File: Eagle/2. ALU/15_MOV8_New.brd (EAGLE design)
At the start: 160 x 100 mm, 7 parts, among them IC3 74LS126N, IC4 74LS126N

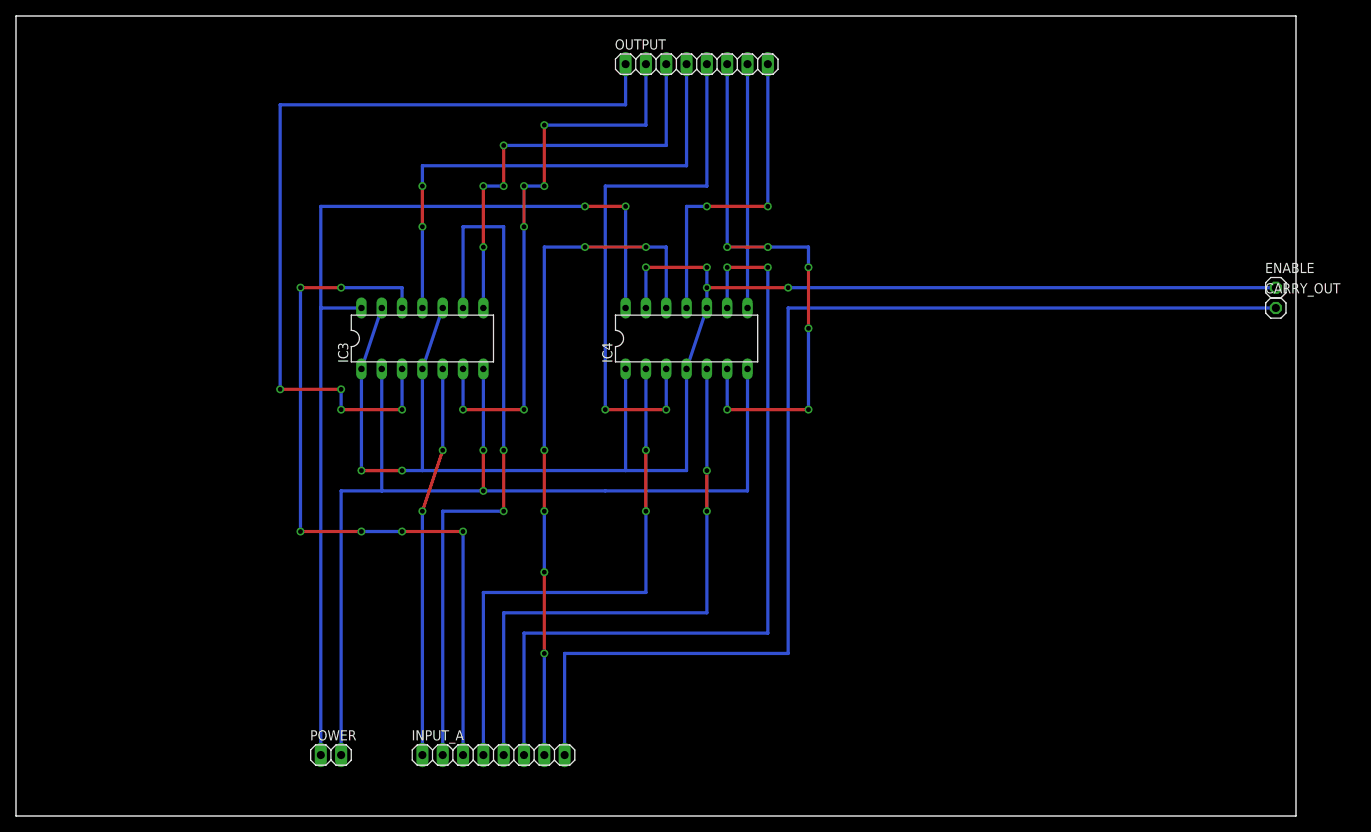
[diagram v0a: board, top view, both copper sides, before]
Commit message: Added new schematics.
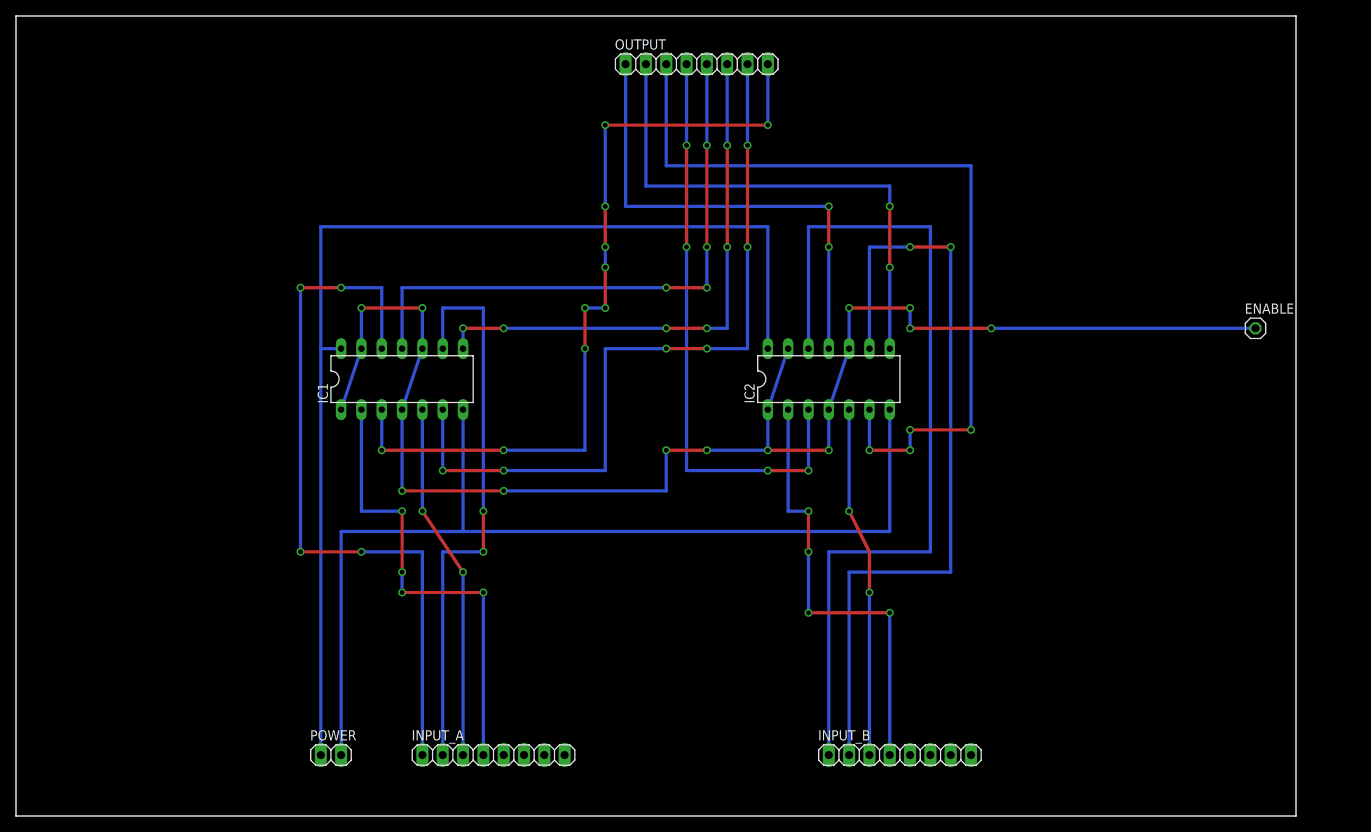
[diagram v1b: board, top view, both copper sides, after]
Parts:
- removed CARRY_OUT: (no value), pinhead:1X01
- removed IC3, IC4: 74LS126N, 74xx-eu:DIL14
- added IC1, IC2: 74LS126N, 74xx-eu:DIL14
- added INPUT_B: (no value), pinhead:1X08
- moved ENABLE 5.68 mm to (154.9, 61.0)
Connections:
- removed net N$20: IC3.12, INPUT_A.3
- removed net N$21: IC4.2, INPUT_A.4
- removed net N$25: IC3.3, OUTPUT.1
- removed net N$26: IC3.6, OUTPUT.2
- removed net N$27: IC3.8, OUTPUT.3
- removed net N$28: IC3.11, OUTPUT.4
- removed net N$29: IC4.3, OUTPUT.5
- removed net N$30: IC4.6, OUTPUT.6
- removed net N$31: IC4.8, OUTPUT.7
- removed net N$32: IC4.11, OUTPUT.8
- removed net N$33: ENABLE.1, IC3.1, IC3.10, IC3.13, IC3.4, IC4.1, IC4.10, IC4.13, IC4.4
- new net N$10: IC1.9, INPUT_A.2
- new net N$12: IC1.2, INPUT_A.4
- new net N$14: IC2.9, INPUT_B.2
- new net N$15: IC2.5, INPUT_B.3
- new net N$16: IC2.2, INPUT_B.4
- new net N$17: ENABLE.1, IC1.1, IC1.10, IC1.13, IC1.4, IC2.1, IC2.10, IC2.13, IC2.4
- new net N$4: IC1.11, OUTPUT.5
- new net N$5: IC2.3, OUTPUT.4
- new net N$6: IC2.6, OUTPUT.3
- new net N$7: IC2.8, OUTPUT.2
- new net N$8: IC2.11, OUTPUT.1
- net GND: now also IC1.7, IC2.7; no longer IC3.2, IC3.7, IC4.7
- net N$1: now also IC1.3, OUTPUT.8; no longer IC3.5, INPUT_A.1
- net N$11: now also IC1.5, INPUT_A.3; no longer IC4.9, INPUT_A.6
- net N$13: now also IC2.12, INPUT_B.1; no longer IC4.12, INPUT_A.7
- net N$2: now also IC1.6, OUTPUT.7; no longer CARRY_OUT.1, INPUT_A.8
- net N$3: now also IC1.8, OUTPUT.6; no longer IC3.9, INPUT_A.2
- net N$9: now also IC1.12, INPUT_A.1; no longer IC4.5, INPUT_A.5
- net VCC: now also IC1.14, IC2.14; no longer IC3.14, IC4.14
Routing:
- net N$33: track 204.4 -> 0.00 mm, vias 6 -> 0
- net N$17: track 0.00 -> 187.1 mm, vias 0 -> 12
- net N$25: track 106.7 -> 0.00 mm, vias 4 -> 0
- net N$6: track 0.00 -> 104.1 mm, vias 0 -> 4
- net N$14: track 0.00 -> 99.1 mm, vias 0 -> 2
- net N$20: track 94.0 -> 0.00 mm, vias 6 -> 0
- net N$5: track 0.00 -> 73.7 mm, vias 0 -> 4
- net N$4: track 0.00 -> 73.7 mm, vias 0 -> 4
- net N$26: track 71.1 -> 0.00 mm, vias 6 -> 0
- net N$10: track 0.00 -> 71.1 mm, vias 0 -> 2
- net N$30: track 68.6 -> 0.00 mm, vias 6 -> 0
- net N$29: track 68.6 -> 0.00 mm, vias 2 -> 0
- net N$21: track 68.6 -> 0.00 mm, vias 2 -> 0
- net N$7: track 0.00 -> 66.0 mm, vias 0 -> 2
- net N$28: track 63.5 -> 0.00 mm, vias 2 -> 0
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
